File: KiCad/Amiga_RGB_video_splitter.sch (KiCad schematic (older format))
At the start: 27 parts, among them J1 DB23_Female-Connector, J2 DB15_Female_HighDensity_Mount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, J3 KMDGX-9S-BS-1, J4 PJ-320A, J5 MSS22D18 3Pin Slide Toggle Sw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, J6 MSS22D18 3Pin Slide Toggle Sw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, U1 THS7374IPWR, U2 74HCT2G17, U3 74HCT2G14, U4 74LVC1GX04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

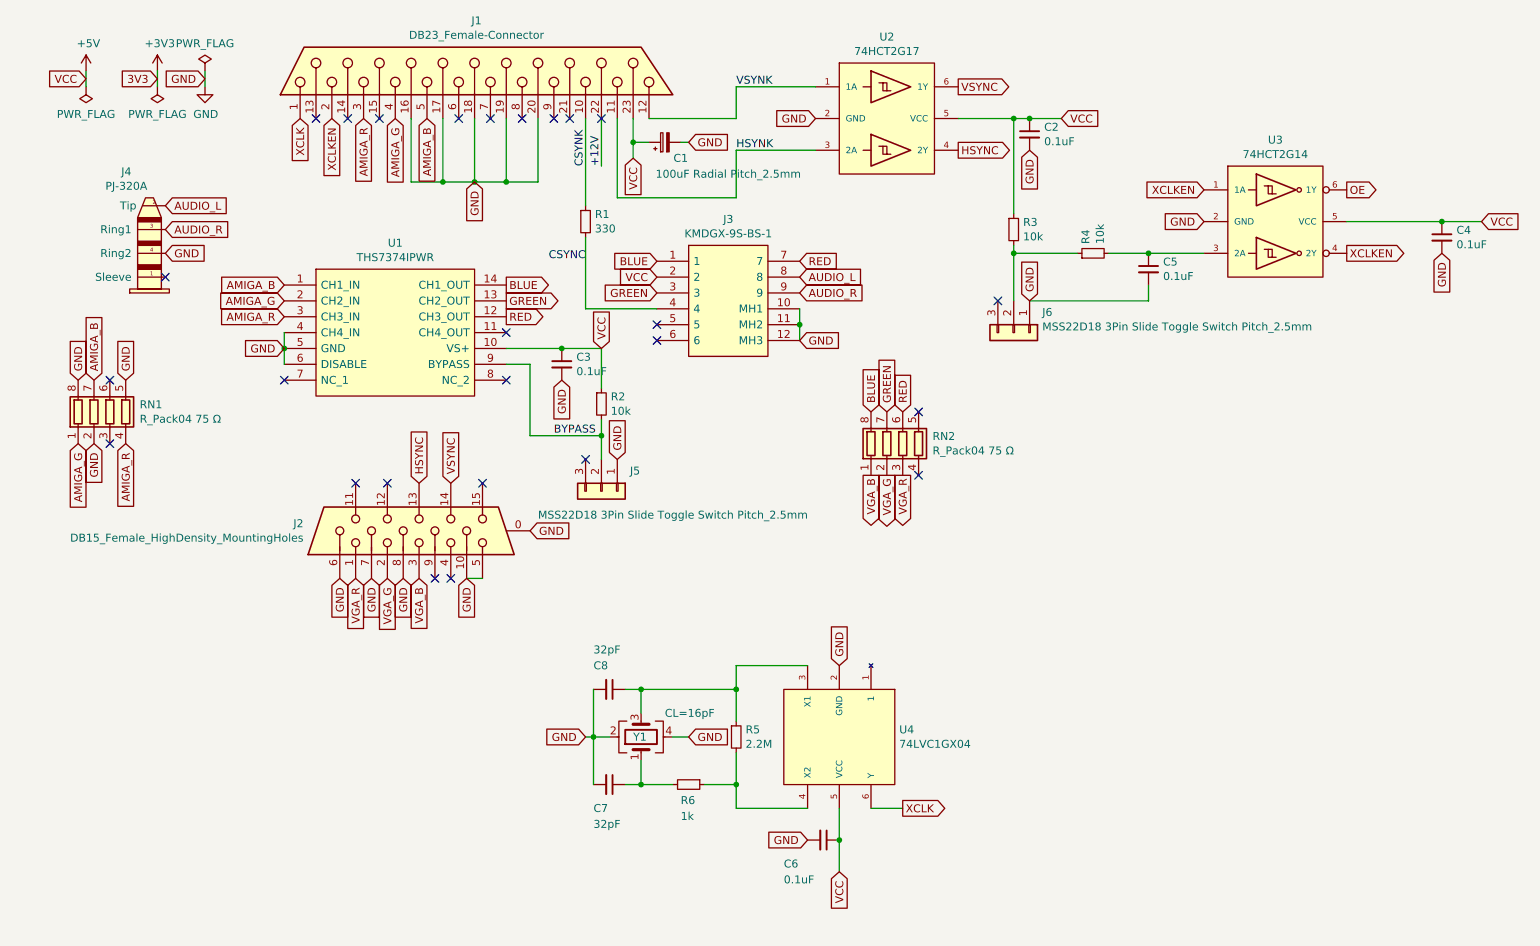
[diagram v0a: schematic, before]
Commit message: Add solder jumper JP1 to the design and route signals XCLKEN and OE to it
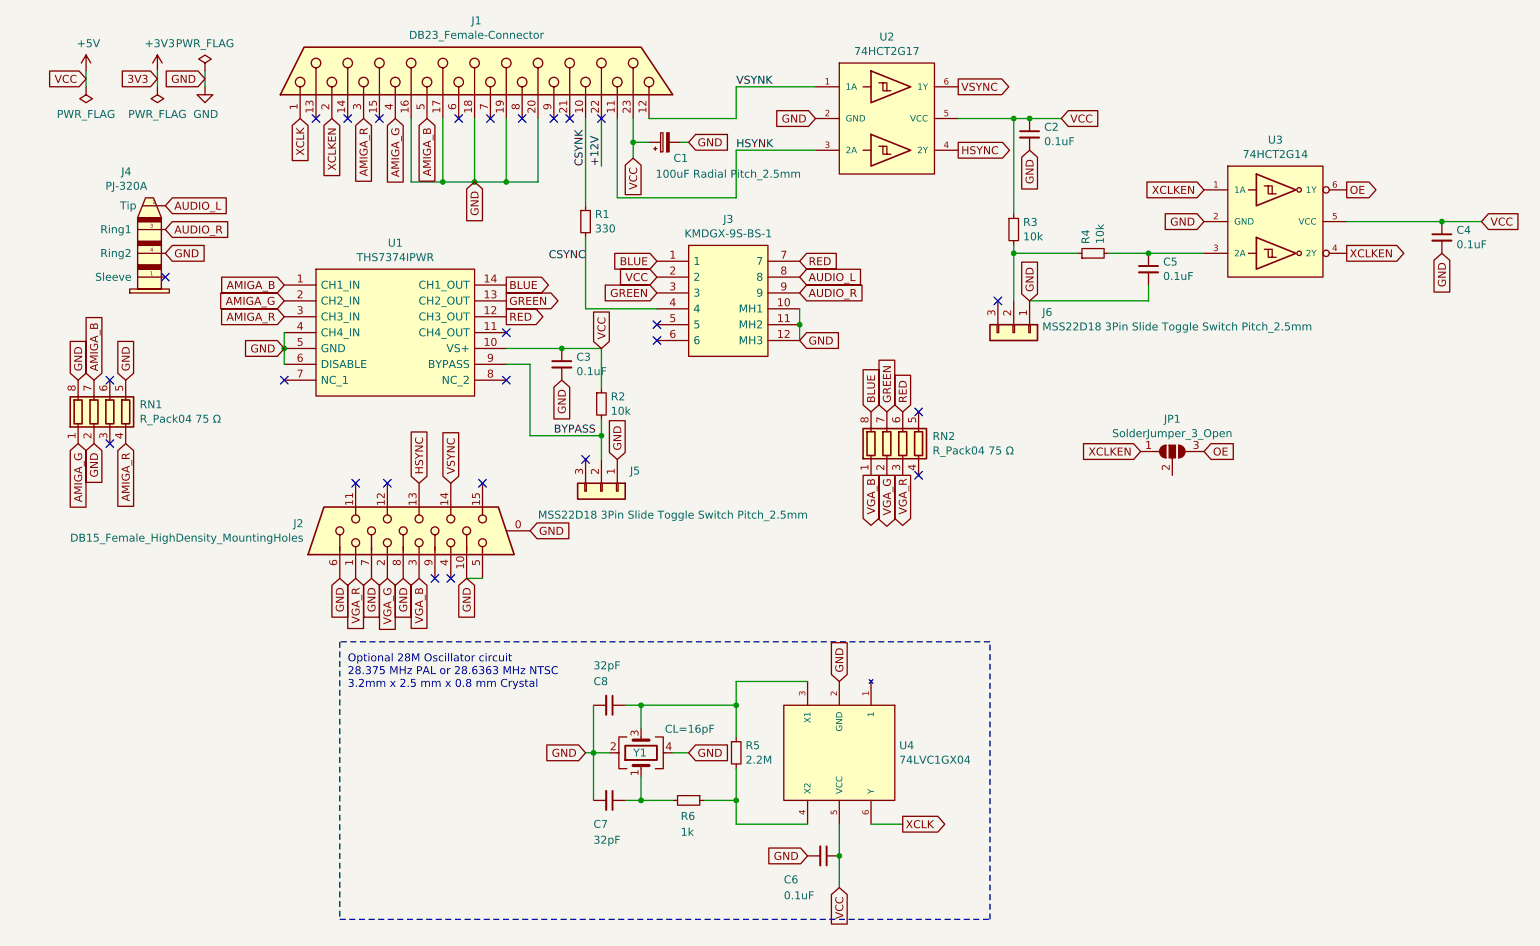
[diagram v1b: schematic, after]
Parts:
- added JP1: SolderJumper_3_Open, Jumper:SolderJumper-3_P1.3mm_Open_RoundedPad1.0x1.5mm_NumberLabels, symbol Jumper:SolderJumper_3_Open
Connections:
- net OE: now also JP1.3 (B)
- net XCLKEN: now also JP1.1 (A)
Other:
- note added: "Optional 28M Oscillator circuit\n28.375 MHz PAL or 28.6363 MHz NTSC\n3.2mm x 2.5 mm x 0.8 mm Crystal"
- moved on the sheet: C6, C7, C8, R5, R6, U4, Y1
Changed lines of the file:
@@
 L Amiga_RGB_video_splitter:74LVC1GX04 U4
 U 1 1 683CA8F1
-P 5900 6600
-F 0 "U4" V 5854 6978 50  0000 L CNN
-F 1 "74LVC1GX04" V 5945 6978 50  0000 L CNN
-F 2 "Package_SO:TSOP-6_1.65x3.05mm_P0.95mm" H 6400 7550 50  0001 C CNN
-F 3 "https://www.mouser.se/datasheet/2/916/74LVC1GX04-2937637.pdf" H 6400 7550 50  0001 C CNN
-	1    5900 6600
+P 5900 6700
+F 0 "U4" V 5854 7078 50  0000 L CNN
+F 1 "74LVC1GX04" V 5945 7078 50  0000 L CNN
+F 2 "Package_SO:TSOP-6_1.65x3.05mm_P0.95mm" H 6400 7650 50  0001 C CNN
+F 3 "https://www.mouser.se/datasheet/2/916/74LVC1GX04-2937637.pdf" H 6400 7650 50  0001 C CNN
+	1    5900 6700
 	0    1    1    0
 $EndComp
-Text GLabel 5900 6150 1    50   Input ~ 0
+Text GLabel 5900 6250 1    50   Input ~ 0
 GND
-Text GLabel 5900 7450 3    50   Input ~ 0
+Text GLabel 5900 7550 3    50   Input ~ 0
 VCC
 $Comp
 L Device:C_Small C6
 U 1 1 683CD4B5
-P 5800 7250
-F 0 "C6" V 5950 7000 50  0000 L CNN
-F 1 "0.1uF" V 6050 7000 50  0000 L CNN
-F 2 "Capacitor_SMD:C_0805_2012Metric_Pad1.18x1.45mm_HandSolder" H 5800 7250 50  0001 C CNN
-F 3 "~" H 5800 7250 50  0001 C CNN
-	1    5800 7250
+P 5800 7350
+F 0 "C6" V 5950 7100 50  0000 L CNN
+F 1 "0.1uF" V 6050 7100 50  0000 L CNN
+F 2 "Capacitor_SMD:C_0805_2012Metric_Pad1.18x1.45mm_HandSolder" H 5800 7350 50  0001 C CNN
+F 3 "~" H 5800 7350 50  0001 C CNN
+	1    5800 7350
 	0    1    1    0
 $EndComp
-Text GLabel 5700 7250 0    50   Input ~ 0
+Text GLabel 5700 7350 0    50   Input ~ 0
 GND
 Wire Wire Line
-	5900 7050 5900 7250
-Connection ~ 5900 7250
+	5900 7150 5900 7350
+Connection ~ 5900 7350
 Wire Wire Line
-	5900 7250 5900 7450
-Text GLabel 6300 7050 2    50   Output ~ 0
+	5900 7350 5900 7550
+Text GLabel 6300 7150 2    50   Output ~ 0
 XCLK
 Wire Wire Line
-	6100 7050 6300 7050
+	6100 7150 6300 7150
 $Comp
 L Device:R_Small R5
 U 1 1 683E0C95
-P 5250 6600
-F 0 "R5" H 5309 6646 50  0000 L CNN
-F 1 "2.2M" H 5309 6555 50  0000 L CNN
-F 2 "Resistor_SMD:R_0603_1608Metric_Pad0.98x0.95mm_HandSolder" H 5250 6600 50  0001 C CNN
-F 3 "~" H 5250 6600 50  0001 C CNN
-	1    5250 6600
+P 5250 6700
+F 0 "R5" H 5309 6746 50  0000 L CNN
+F 1 "2.2M" H 5309 6655 50  0000 L CNN
+F 2 "Resistor_SMD:R_0603_1608Metric_Pad0.98x0.95mm_HandSolder" H 5250 6700 50  0001 C CNN
+F 3 "~" H 5250 6700 50  0001 C CNN
+	1    5250 6700
 	1    0    0    -1
 $EndComp
 Wire Wire Line
-	5250 6150 5700 6150
+	5250 6250 5700 6250
 Wire Wire Line
-	5700 7050 5250 7050
+	5700 7150 5250 7150
 $Comp
 L Device:Crystal_GND24 Y1
 U 1 1 683ED2B8
-P 4650 6600
-F 0 "Y1" V 4650 6650 50  0000 R CNN
-F 1 "CL=16pF" V 4800 6450 50  0000 R CNN
-F 2 "Crystal:Crystal_SMD_SeikoEpson_FA238-4Pin_3.2x2.5mm" H 4650 6600 50  0001 C CNN
-F 3 "~" H 4650 6600 50  0001 C CNN
-	1    4650 6600
+P 4650 6700
+F 0 "Y1" V 4650 6750 50  0000 R CNN
+F 1 "CL=16pF" V 4800 6550 50  0000 R CNN
+F 2 "Crystal:Crystal_SMD_SeikoEpson_FA238-4Pin_3.2x2.5mm" H 4650 6700 50  0001 C CNN
+F 3 "~" H 4650 6700 50  0001 C CNN
+	1    4650 6700
 	0    -1   -1   0
 $EndComp
-Text GLabel 4950 6600 2    50   Input ~ 0
+Text GLabel 4950 6700 2    50   Input ~ 0
 GND
 Wire Wire Line
-	4650 6450 4650 6300
+	4650 6550 4650 6400
 Wire Wire Line
-	4650 6750 4650 6900
-Text GLabel 4300 6600 0    50   Input ~ 0
+	4650 6850 4650 7000
+Text GLabel 4300 6700 0    50   Input ~ 0
 GND
 $Comp
 L Device:R_Small R6
 U 1 1 683F6DEA
-P 4950 6900
-F 0 "R6" V 5050 6850 50  0000 L CNN
-F 1 "1k" V 5150 6850 50  0000 L CNN
-F 2 "Resistor_SMD:R_0603_1608Metric_Pad0.98x0.95mm_HandSolder" H 4950 6900 50  0001 C CNN
-F 3 "~" H 4950 6900 50  0001 C CNN
-	1    4950 6900
+P 4950 7000
+F 0 "R6" V 5050 6950 50  0000 L CNN
+F 1 "1k" V 5150 6950 50  0000 L CNN
+F 2 "Resistor_SMD:R_0603_1608Metric_Pad0.98x0.95mm_HandSolder" H 4950 7000 50  0001 C CNN
+F 3 "~" H 4950 7000 50  0001 C CNN
+	1    4950 7000
 	0    1    1    0
 $EndComp
 Wire Wire Line
-	5250 6700 5250 6900
+	5250 6800 5250 7000
 Wire Wire Line
-	5250 6150 5250 6300
+	5250 6250 5250 6400
 Wire Wire Line
-	4650 6300 5250 6300
-Connection ~ 5250 6300
+	4650 6400 5250 6400
+Connection ~ 5250 6400
 Wire Wire Line
-	5250 6300 5250 6500
+	5250 6400 5250 6600
 Wire Wire Line
-	5050 6900 5250 6900
-Connection ~ 5250 6900
+	5050 7000 5250 7000
+Connection ~ 5250 7000
 Wire Wire Line
-	5250 6900 5250 7050
+	5250 7000 5250 7150
 Wire Wire Line
-	4850 6900 4650 6900
+	4850 7000 4650 7000
 $Comp
 L Device:C_Small C8
 U 1 1 68407AAC
-P 4450 6300
-F 0 "C8" V 4300 6200 50  0000 L CNN
-F 1 "32pF" V 4200 6200 50  0000 L CNN
-F 2 "Capacitor_SMD:C_0603_1608Metric_Pad1.08x0.95mm_HandSolder" H 4450 6300 50  0001 C CNN
-F 3 "~" H 4450 6300 50  0001 C CNN
-	1    4450 6300
+P 4450 6400
+F 0 "C8" V 4300 6300 50  0000 L CNN
+F 1 "32pF" V 4200 6300 50  0000 L CNN
+F 2 "Capacitor_SMD:C_0603_1608Metric_Pad1.08x0.95mm_HandSolder" H 4450 6400 50  0001 C CNN
+F 3 "~" H 4450 6400 50  0001 C CNN
+	1    4450 6400
 	0    1    1    0
 $EndComp
@@
 L Device:C_Small C7
 U 1 1 68409377
-P 4450 6900
-F 0 "C7" V 4600 6800 50  0000 L CNN
-F 1 "32pF" V 4700 6800 50  0000 L CNN
-F 2 "Capacitor_SMD:C_0603_1608Metric_Pad1.08x0.95mm_HandSolder" H 4450 6900 50  0001 C CNN
-F 3 "~" H 4450 6900 50  0001 C CNN
-	1    4450 6900
+P 4450 7000
+F 0 "C7" V 4600 6900 50  0000 L CNN
+F 1 "32pF" V 4700 6900 50  0000 L CNN
+F 2 "Capacitor_SMD:C_0603_1608Metric_Pad1.08x0.95mm_HandSolder" H 4450 7000 50  0001 C CNN
+F 3 "~" H 4450 7000 50  0001 C CNN
+	1    4450 7000
 	0    1    1    0
 $EndComp
 Wire Wire Line
-	4550 6300 4650 6300
-Connection ~ 4650 6300
+	4550 6400 4650 6400
+Connection ~ 4650 6400
 Wire Wire Line
-	4550 6900 4650 6900
-Connection ~ 4650 6900
+	4550 7000 4650 7000
+Connection ~ 4650 7000
 Wire Wire Line
-	4950 6600 4850 6600
+	4950 6700 4850 6700
 Wire Wire Line
-	4350 6300 4350 6600
+	4350 6400 4350 6700
 Wire Wire Line
-	4450 6600 4350 6600
-Connection ~ 4350 6600
+	4450 6700 4350 6700
+Connection ~ 4350 6700
 Wire Wire Line
-	4350 6600 4350 6900
+	4350 6700 4350 7000
 Wire Wire Line
-	4350 6600 4300 6600
+	4350 6700 4300 6700
+Wire Notes Line
+	6850 7750 6850 6000
+Wire Notes Line
+	6850 6000 2750 6000
+Wire Notes Line
+	2750 6000 2750 7750
+Wire Notes Line
+	2750 7750 6850 7750
+Text Notes 2800 6300 0    50   ~ 0
+Optional 28M Oscillator circuit\n28.375 MHz PAL or 28.6363 MHz NTSC\n3.2mm x 2.5 mm x 0.8 mm Crystal
+$Comp
+L Jumper:SolderJumper_3_Open JP1
+U 1 1 68426716
+P 8000 4800
+F 0 "JP1" H 8000 5005 50  0000 C CNN
+F 1 "SolderJumper_3_Open" H 8000 4914 50  0000 C CNN
+F 2 "Jumper:SolderJumper-3_P1.3mm_Open_RoundedPad1.0x1.5mm_NumberLabels" H 8000 4800 50  0001 C CNN
+F 3 "~" H 8000 4800 50  0001 C CNN
+	1    8000 4800
+	1    0    0    -1
+$EndComp
+Text GLabel 7800 4800 0    50   Input ~ 0
+XCLKEN
+Text GLabel 8200 4800 2    50   Input ~ 0
+OE
 $EndSCHEMATC

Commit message: Add four PinHeader_1x03_P2.54mm for support structure, fix of edge cuts for better fit plastic shells
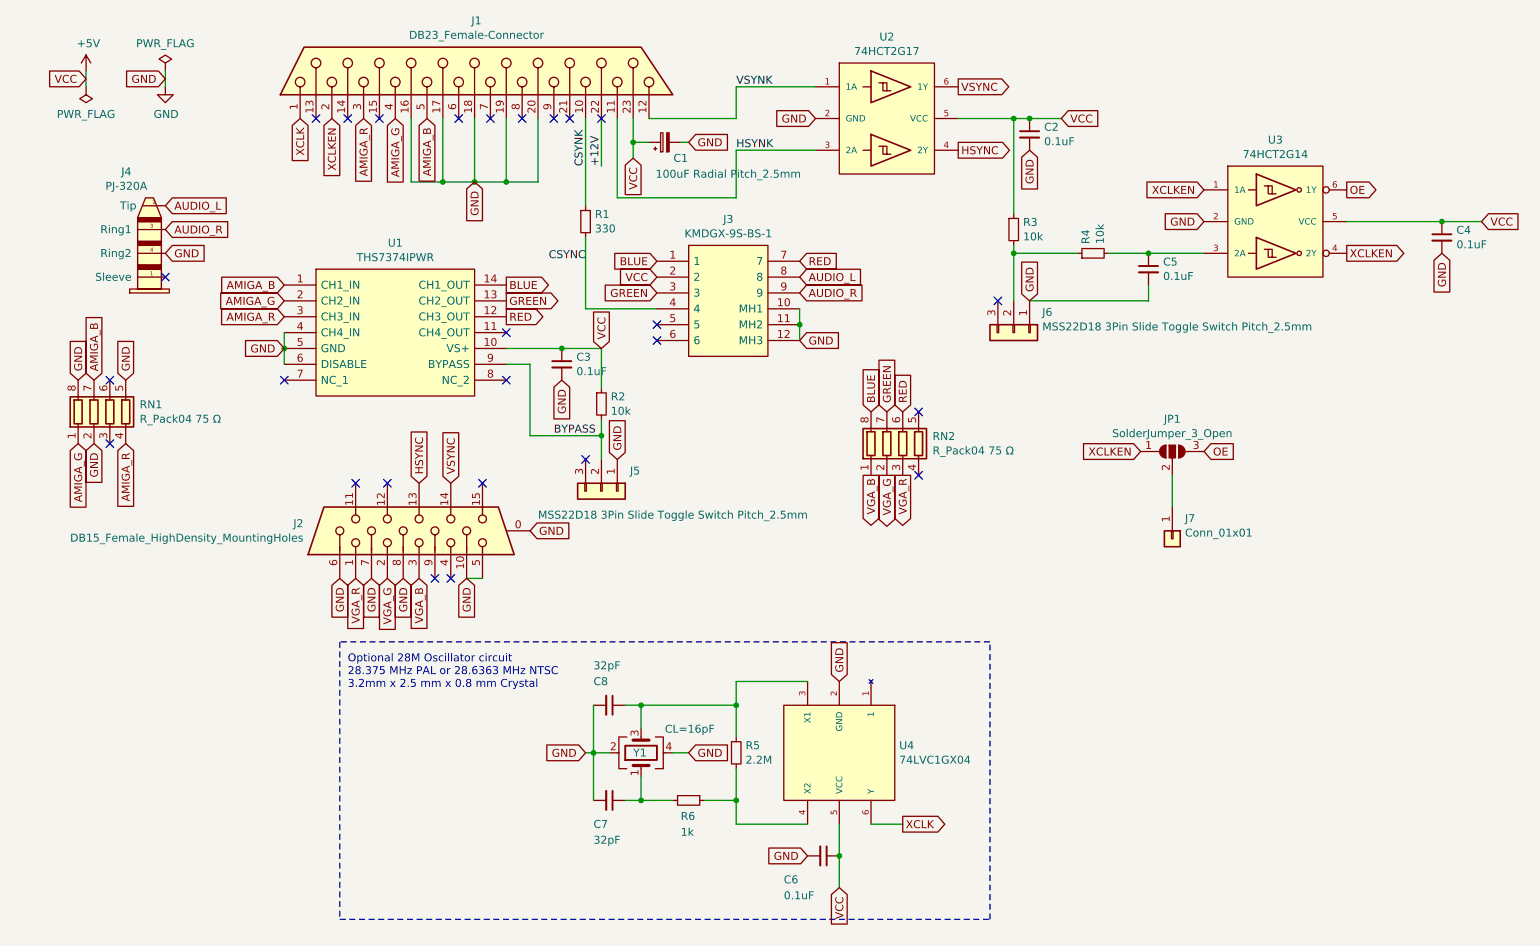
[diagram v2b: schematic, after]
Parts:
- added J7: Conn_01x01, Connector_PinHeader_2.54mm:PinHeader_1x01_P2.54mm_Vertical, symbol Connector_Generic:Conn_01x01
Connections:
- net at JP1.2 (C): now also J7.1 (Pin_1)
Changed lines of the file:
@@
 $EndDescr
-$Comp
-L power:PWR_FLAG #FLG0101
-U 1 1 5EB341E8
-P 1600 2500
-F 0 "#FLG0101" H 1600 2575 50  0001 C CNN
-F 1 "PWR_FLAG" H 1600 2673 50  0000 C CNN
-F 2 "" H 1600 2500 50  0001 C CNN
-F 3 "~" H 1600 2500 50  0001 C CNN
-	1    1600 2500
-	-1   0    0    1
-$EndComp
-Wire Wire Line
-	1600 2400 1600 2500
 $Comp
 L power:GND #PWR0102
 U 1 1 5EB362B9
-P 1900 2500
-F 0 "#PWR0102" H 1900 2250 50  0001 C CNN
-F 1 "GND" H 1905 2327 50  0000 C CNN
-F 2 "" H 1900 2500 50  0001 C CNN
-F 3 "" H 1900 2500 50  0001 C CNN
-	1    1900 2500
+P 1650 2500
+F 0 "#PWR0102" H 1650 2250 50  0001 C CNN
+F 1 "GND" H 1655 2327 50  0000 C CNN
+F 2 "" H 1650 2500 50  0001 C CNN
+F 3 "" H 1650 2500 50  0001 C CNN
+	1    1650 2500
 	1    0    0    -1
 $EndComp
@@
 L power:PWR_FLAG #FLG0102
 U 1 1 5EB368E6
-P 1900 2400
-F 0 "#FLG0102" H 1900 2475 50  0001 C CNN
-F 1 "PWR_FLAG" H 1900 2573 50  0000 C CNN
-F 2 "" H 1900 2400 50  0001 C CNN
-F 3 "~" H 1900 2400 50  0001 C CNN
-	1    1900 2400
-	1    0    0    -1
-$EndComp
-Wire Wire Line
-	1900 2400 1900 2500
-Text GLabel 1900 2450 0    50   Input ~ 0
-GND
-Text GLabel 1600 2450 0    50   Input ~ 0
-3V3
-$Comp
-L power:+3V3 #PWR0101
-U 1 1 644304C8
-P 1600 2400
-F 0 "#PWR0101" H 1600 2250 50  0001 C CNN
-F 1 "+3V3" H 1615 2573 50  0000 C CNN
-F 2 "" H 1600 2400 50  0001 C CNN
-F 3 "" H 1600 2400 50  0001 C CNN
-	1    1600 2400
-	1    0    0    -1
-$EndComp
+P 1650 2400
+F 0 "#FLG0102" H 1650 2475 50  0001 C CNN
+F 1 "PWR_FLAG" H 1650 2573 50  0000 C CNN
+F 2 "" H 1650 2400 50  0001 C CNN
+F 3 "~" H 1650 2400 50  0001 C CNN
+	1    1650 2400
+	1    0    0    -1
+$EndComp
+Wire Wire Line
+	1650 2400 1650 2500
+Text GLabel 1650 2450 0    50   Input ~ 0
+GND
 $Comp
 L power:+5V #PWR0103
@@
 Text GLabel 8200 4800 2    50   Input ~ 0
 OE
+$Comp
+L Connector_Generic:Conn_01x01 J7
+U 1 1 6843C799
+P 8000 5350
+F 0 "J7" V 7872 5430 50  0000 L CNN
+F 1 "Conn_01x01" V 7963 5430 50  0000 L CNN
+F 2 "Connector_PinHeader_2.54mm:PinHeader_1x01_P2.54mm_Vertical" H 8000 5350 50  0001 C CNN
+F 3 "~" H 8000 5350 50  0001 C CNN
+	1    8000 5350
+	0    1    1    0
+$EndComp
+Wire Wire Line
+	8000 4950 8000 5150
 $EndSCHEMATC

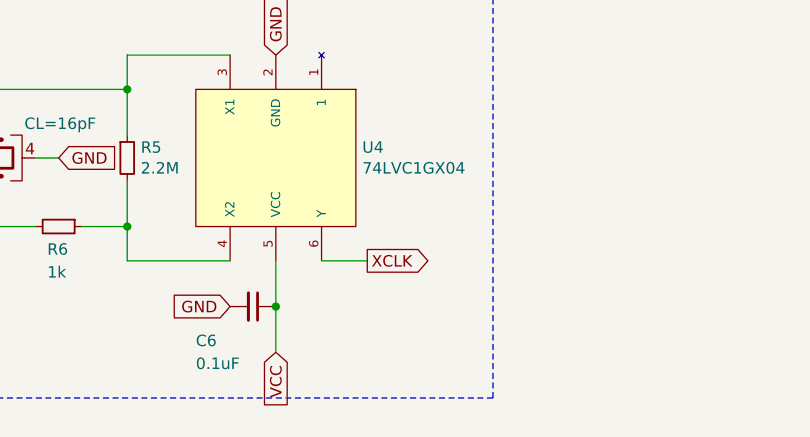
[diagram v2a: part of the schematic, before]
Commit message: Add damping 150 Ohm series resistor on XCLK out, bump to Rev. C
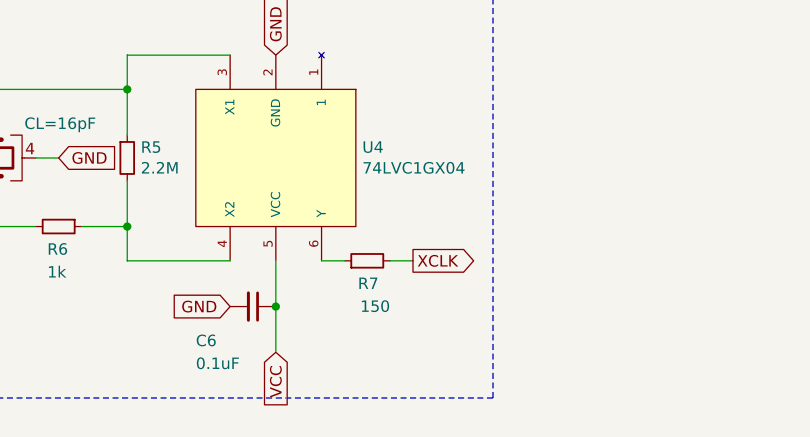
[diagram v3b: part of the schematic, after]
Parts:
- added R7: 150, Resistor_SMD:R_1206_3216Metric_Pad1.30x1.75mm_HandSolder, symbol Device:R_Small
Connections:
- net XCLK: now also R7.2; no longer U4.6 (Y)
- new net: R7.1, U4.6 (Y)
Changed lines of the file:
@@
 Wire Wire Line
 	5900 7350 5900 7550
-Text GLabel 6300 7150 2    50   Output ~ 0
+Text GLabel 6500 7150 2    50   Output ~ 0
 XCLK
-Wire Wire Line
-	6100 7150 6300 7150
 $Comp
 L Device:R_Small R5
@@
 Wire Wire Line
 	8000 4950 8000 5150
+$Comp
+L Device:R_Small R7
+U 1 1 699199BB
+P 6300 7150
+F 0 "R7" V 6200 7100 50  0000 L CNN
+F 1 "150" V 6100 7050 50  0000 L CNN
+F 2 "Resistor_SMD:R_1206_3216Metric_Pad1.30x1.75mm_HandSolder" H 6300 7150 50  0001 C CNN
+F 3 "~" H 6300 7150 50  0001 C CNN
+	1    6300 7150
+	0    -1   -1   0
+$EndComp
+Wire Wire Line
+	6100 7150 6200 7150
+Wire Wire Line
+	6400 7150 6500 7150
 $EndSCHEMATC
